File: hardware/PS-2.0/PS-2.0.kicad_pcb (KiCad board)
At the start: 2 copper layers, 119.7 x 199.4 mm, 52 parts, among them J1 PinSocket_02x16_P2.54mm_Verti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, J2 Conn_01x05, J3 Conn_01x05, J8 Conn_01x02, J9 Conn_01x02, K1 RAYEX-L90, K2 RAYEX-L90, Q1 IRFPE50, Q2 IRFPE50, Q3 IRFPE50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

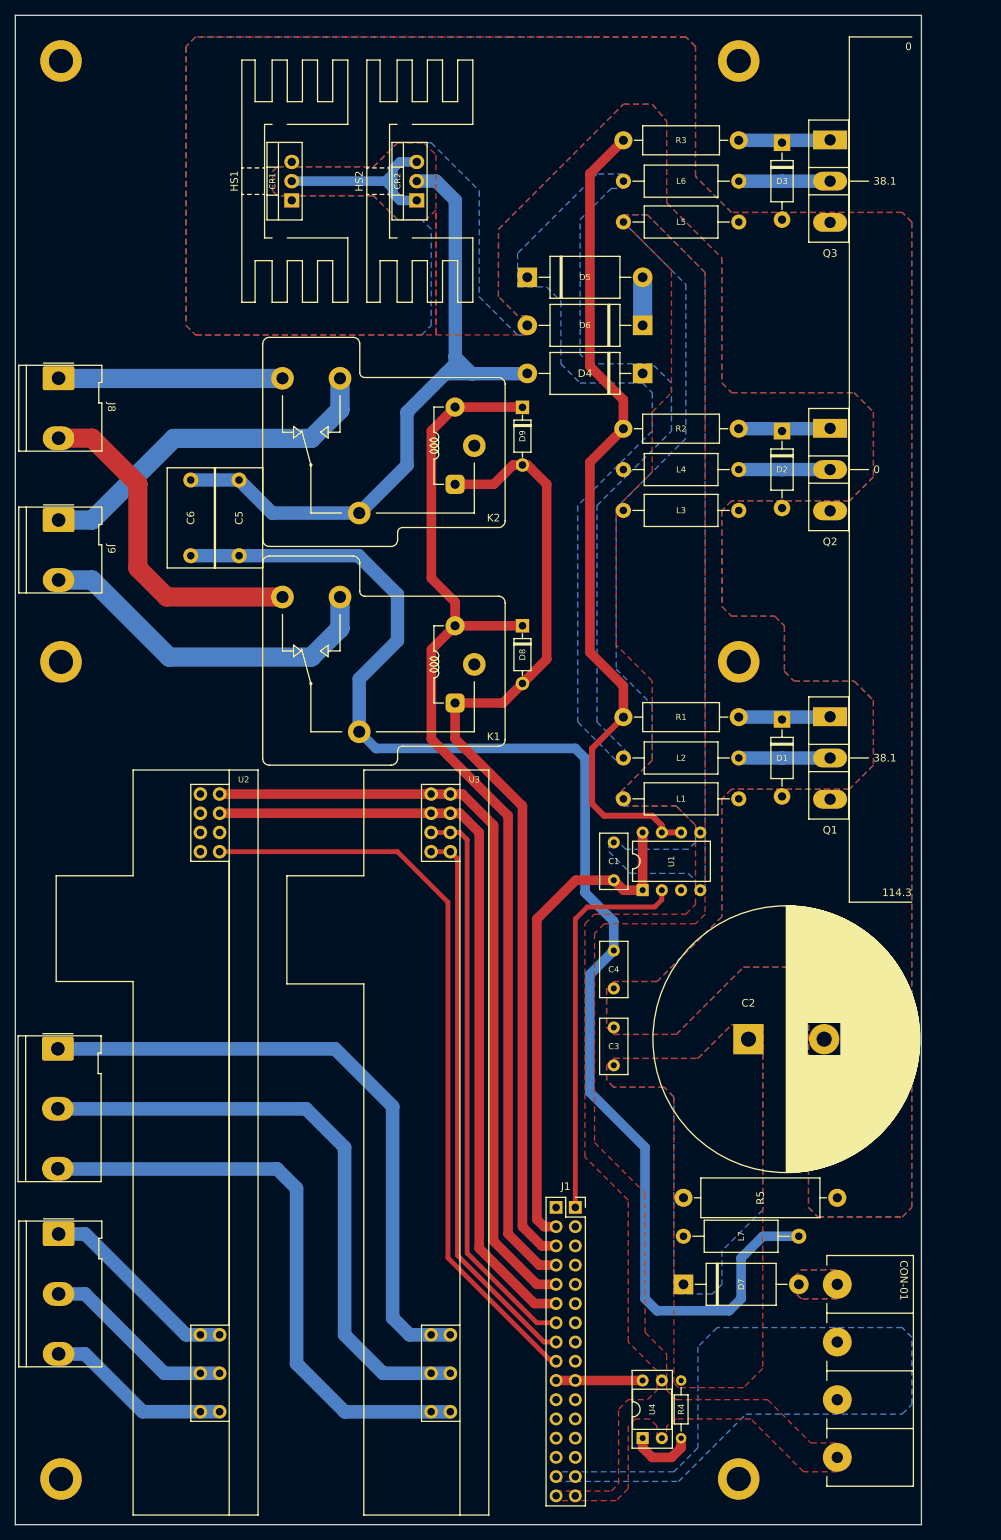
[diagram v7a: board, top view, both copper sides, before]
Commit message: deleted:    hardware/CTL-1.0/CTL-1.0-backups/CTL-1.0-2025-06-04_115049.zip 	deleted:    hardware/CTL-1.0/CTL-1.0-backups/CTL-1.0-2025-06-04_132910.zip 	deleted:    hardware/CTL-1.0/CTL-1.0-backups/CTL-1.0-2025-06-05_142549.zip 	deleted:    hardware/CTL-1.0/CTL-1.0-backups/CTL-1.0-2025-06-05_143053.zip 	deleted:    hardware/CTL-1.0/CTL-1.0-backups/CTL-1.0-2025-06-05_144242.zip 	new file:   hardware/CTL-1.0/CTL-1.0-backups/CTL-1.0-2025-08-01_111317.zip 	new file:   hardware/CTL-1.0/CTL-1.0-backups/CTL-1.0-2025-08-01_113544.zip 	new file:   hardware/CTL-1.0/CTL-1.0-backups/CTL-1.0-2025-08-01_114559.zip 	new file:   hardware/CTL-1.0/CTL-1.0-backups/CTL-1.0-2025-08-01_115359.zip 	new file:   hardware/CTL-1.0/CTL-1.0-backups/CTL-1.0-2025-08-01_115915.zip 	new file:   hardware/CTL-1.0/CTL-1.0-backups/CTL-1.0-2025-08-01_131607.zip 	modified:   hardware/CTL-1.0/CTL-1.0.kicad_pcb 	modified:   hardware/CTL-1.0/CTL-1.0.kicad_sch 	renamed:    hardware/CTL-1.0/CTL-1.0-backups/CTL-1.0-2025-06-05_144757.zip -> hardware/CTL-1.2/CTL-1.0-backups/CTL-1.0-2025-06-05_145506.zip 	new file:   hardware/CTL-1.2/CTL-1.0-backups/CTL-1.0-2025-06-10_100335.zip 	new file:   hardware/CTL-1.2/CTL-1.0-backups/CTL-1.0-2025-06-12_095314.zip 	new file:   hardware/CTL-1.2/CTL-1.0-backups/CTL-1.0-2025-07-03_115731.zip 	new file:   hardware/CTL-1.2/CTL-1.0-backups/CTL-1.0-2025-07-16_143147.zip 	new file:   hardware/CTL-1.2/CTL-1.0-backups/CTL-1.0-2025-07-24_151142.zip 	new file:   hardware/CTL-1.2/CTL-1.0-backups/CTL-1.0-2025-07-24_172002.zip 	new file:   hardware/CTL-1.2/CTL-1.0-backups/CTL-1.0-2025-07-25_175122.zip 	new file:   hardware/CTL-1.2/CTL-1.0-backups/CTL-1.0-2025-07-26_120011.zip 	new file:   hardware/CTL-1.2/CTL-1.0-backups/CTL-1.0-2025-07-26_120808.zip 	new file:   hardware/CTL-1.2/CTL-1.0-backups/CTL-1.0-2025-07-28_094555.zip 	new file:   hardware/CTL-1.2/CTL-1.0-backups/CTL-1.0-2025-07-28_104747.zip 	new file:   hardware/CTL-1.2/CTL-1.0-backups/CTL-1.0-2025-07-28_112613.zip 	new file:   ha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
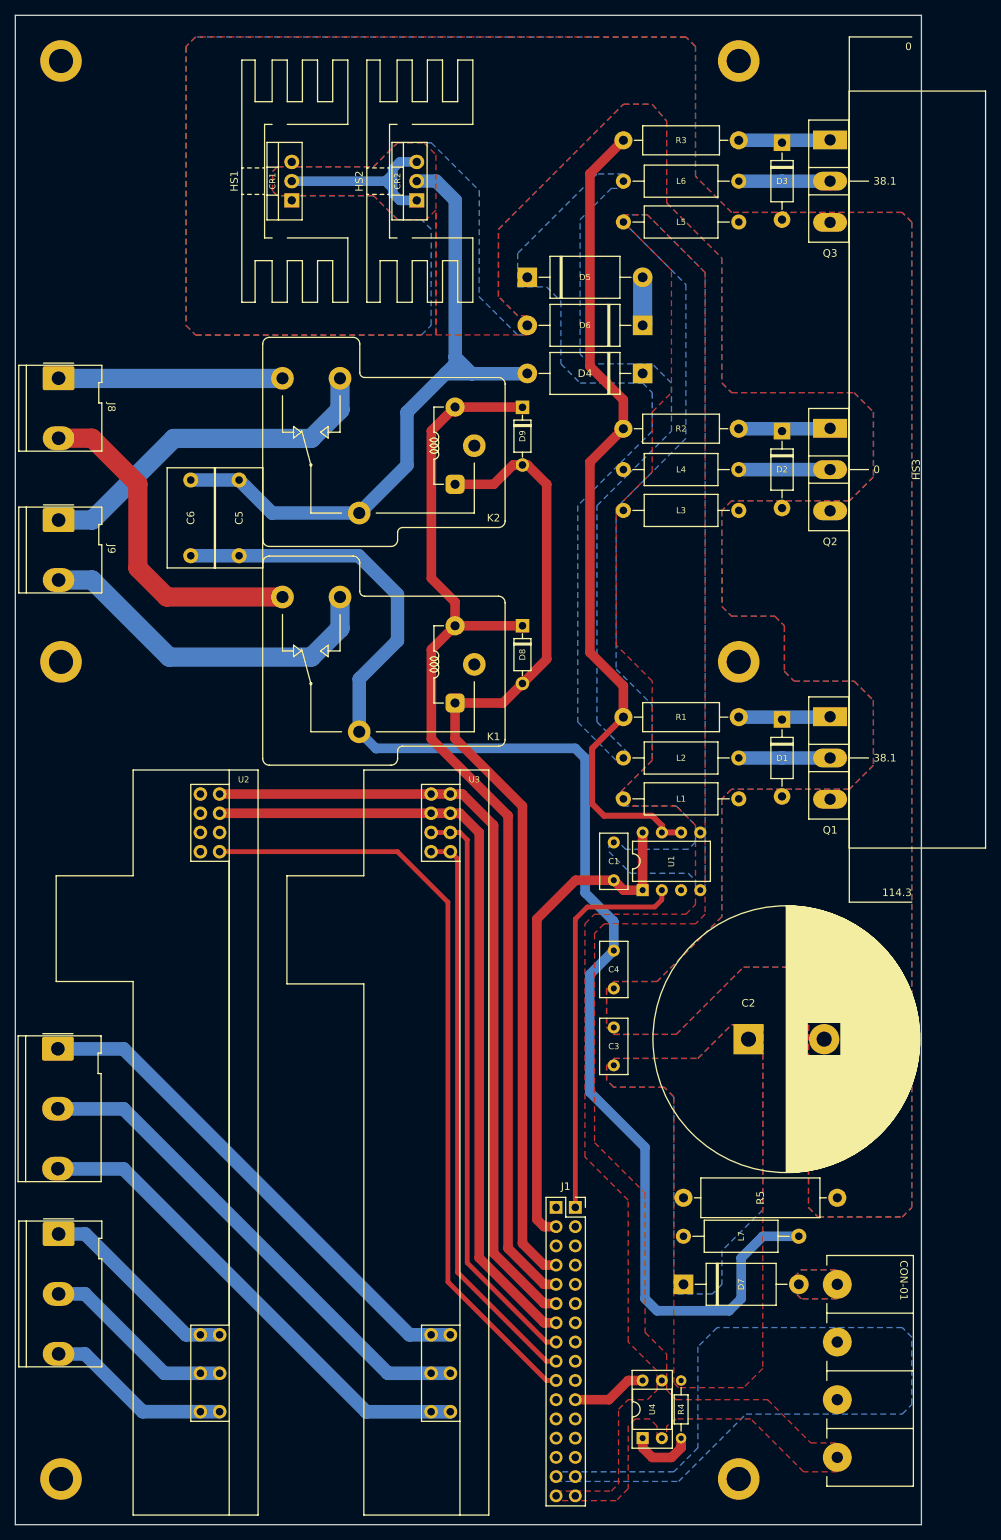
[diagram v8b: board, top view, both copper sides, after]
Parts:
- added HS3: Heatsink, Heatsink:Heatsink_Custom_10x18x50, F.Cu at (230.8, 89.2)
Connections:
- net VDD renamed /PWM-EN
- J1 pad 10: /OPTO -> /REM
- J1 pad 11: unconnected-(J1-Pin_11-Pad11) -> /OPTO
- J1 pad 3: /RLY-A -> unconnected-(J1-Pin_3-Pad3)
- J1 pad 4: /RLY-K -> /RLY-A
- J1 pad 5: /+5V -> /RLY-K
- J1 pad 6: GND -> /+5V
- J1 pad 7: /MSD1 -> GND
- J1 pad 8: /MSD2 -> /MSD1
- J1 pad 9: /REM -> /MSD2
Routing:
- net Net-(J3-Pin_1): track 83.8 -> 67.5 mm
- net Net-(J3-Pin_3): track 80.8 -> 66.3 mm
- net Net-(J3-Pin_5): track 78.7 -> 65.1 mm
- net /REM: track 99.9 -> 102.8 mm
- net /RLY-A: track 128.9 -> 131.3 mm
- net /MSD2: track 74.0 -> 76.4 mm
- net /RLY-K: track 142.5 -> 144.7 mm
- net /+5V: track 103.5 -> 105.4 mm
- net GND: track 103.5 -> 105.3 mm
- net /MSD1: track 75.3 -> 77.1 mm
- net /OPTO: track 11.4 -> 9.94 mm
